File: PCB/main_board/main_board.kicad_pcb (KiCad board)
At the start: 2 copper layers, 57 x 29 mm, 49 parts, among them CN1 XT30PW-M, CN2 XT30PW-M, U1 XT30PW-F, U3 W25N01GVZEIG_C907680, U4 INA226, U5 INA226, U6 RP2040, U7 AZ1117-3.3, X1 X322512MSB4SI

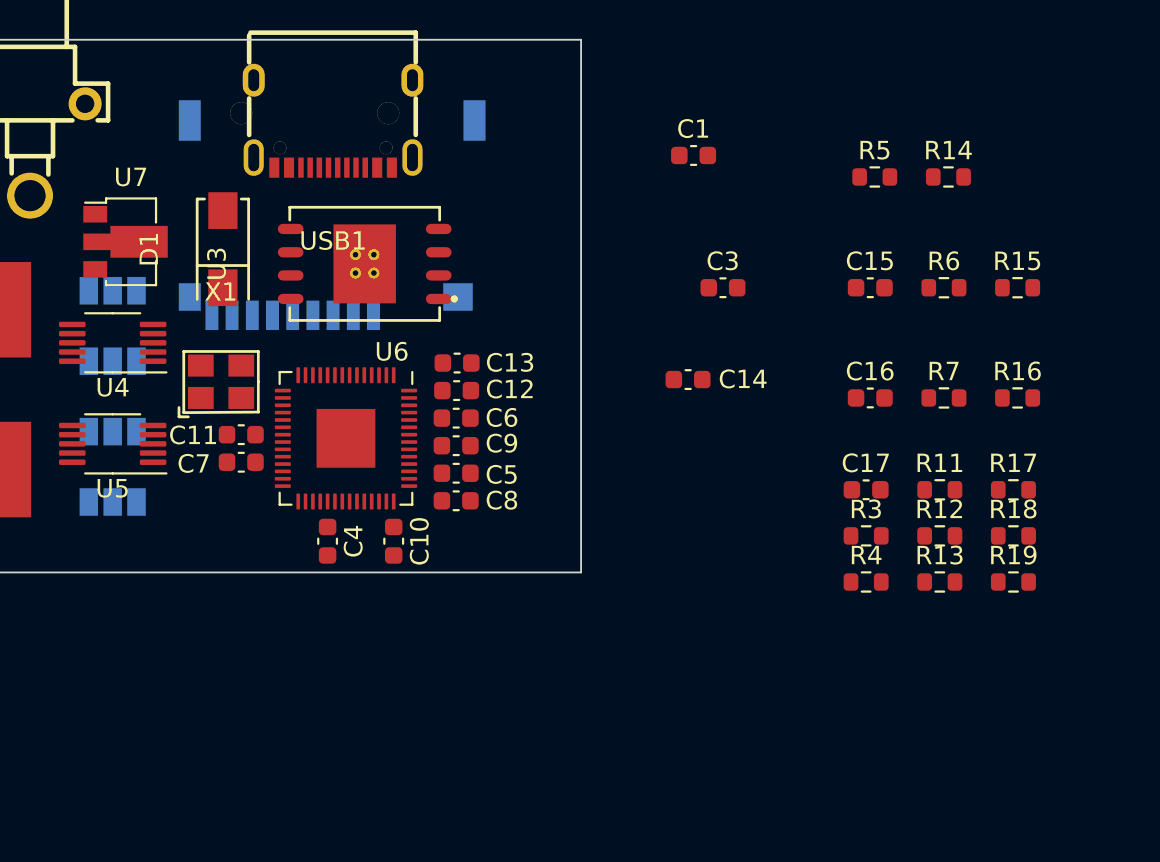
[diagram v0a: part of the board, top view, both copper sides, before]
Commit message: Add EEPROM to mcu; Change R and C to 0402
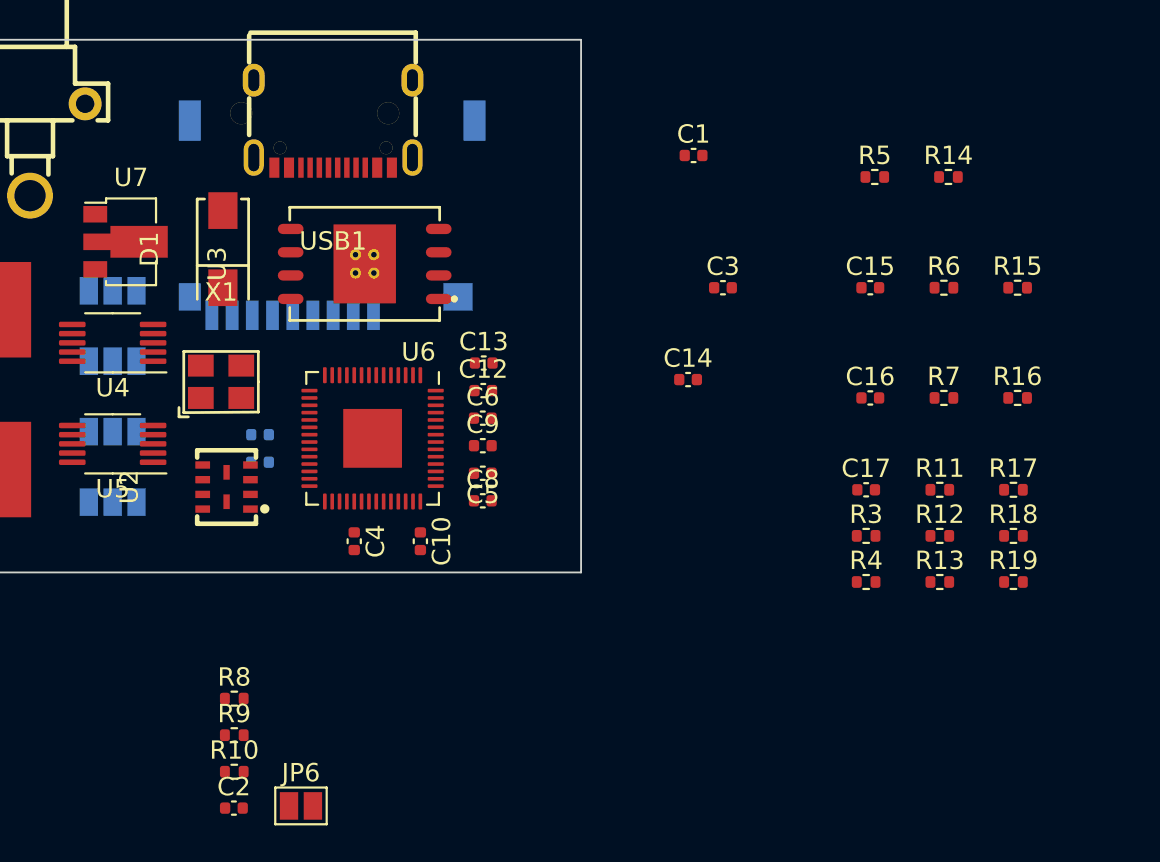
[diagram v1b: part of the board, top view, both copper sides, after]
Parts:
- added C2: 100n, Capacitor_SMD:C_0402_1005Metric, F.Cu at (63.6, 66.3)
- added JP6: SolderJumper_2_Open, Jumper:SolderJumper-2_P1.3mm_Open_Pad1.0x1.5mm, F.Cu at (67.2, 66.2)
- added R10: 1k, Resistor_SMD:R_0402_1005Metric, F.Cu at (63.6, 64.3)
- added R8: 10k, Resistor_SMD:R_0402_1005Metric, F.Cu at (63.6, 60.4)
- added R9: 10k, Resistor_SMD:R_0402_1005Metric, F.Cu at (63.6, 62.4)
- added U2: W25Q32JVUUIQ, pcb_lib:USON-8_L4.0-W3.0-P0.80-BL_WINBOND_UU, F.Cu at (63.2, 48.9)
- C1, C10, C12, C13, C14, C15, C16, C17, C3, C4, C5, C6, C8, C9: footprint Capacitor_SMD:C_0603_1608Metric -> Capacitor_SMD:C_0402_1005Metric
- C11, C7: footprint Capacitor_SMD:C_0603_1608Metric -> Capacitor_SMD:C_0402_1005Metric; moved to B.Cu
- CN1, CN2: footprint easyeda2kicad:CONN-TH_XT30PW-M -> pcb_lib:CONN-TH_XT30PW-M
- Card1: footprint easyeda2kicad:TF-SMD_XKTF-015-N -> pcb_lib:TF-SMD_XKTF-015-N
- D1: footprint easyeda2kicad:SMA_L4.3-W2.5-LS5.0-RD -> pcb_lib:SMA_L4.3-W2.5-LS5.0-RD
- R1, R2: footprint easyeda2kicad:R3920 -> pcb_lib:R3920
- R11, R12, R13, R14, R15, R16, R17, R18, R19, R3, R4, R5, R6, R7: footprint Resistor_SMD:R_0603_1608Metric -> Resistor_SMD:R_0402_1005Metric
- U1: footprint easyeda2kicad:CONN-TH_XT30PW-F-1 -> pcb_lib:CONN-TH_XT30PW-F-1
- U3: footprint easyeda2kicad:WSON-8_L8.0-W6.10-P1.27-BL-EP -> pcb_lib:WSON-8_L8.0-W6.10-P1.27-BL-EP
- USB1: footprint easyeda2kicad:USB-C-SMD_TYPE-C-6PIN-2MD-073 -> pcb_lib:USB-C-SMD_TYPE-C-6PIN-2MD-073
- X1: footprint easyeda2kicad:OSC-SMD_4P-L3.2-W2.5-BL -> pcb_lib:OSC-SMD_4P-L3.2-W2.5-BL
- moved C10 1.45 mm to (73.8, 51.8)
- moved C12 1.45 mm to (77.2, 43.6)
- moved C13 1.45 mm to (77.2, 42.1)
- moved C4 1.45 mm to (70.2, 51.8)
- moved C5 1.45 mm to (77.2, 48.1)
- moved C6 1.45 mm to (77.2, 45.1)
- moved C8 1.45 mm to (77.2, 49.6)
- moved C9 1.45 mm to (77.2, 46.6)
- moved U6 1.45 mm to (71.2, 46.2)
- moved C11 1.02 mm to (65.0, 46.0), turned to 0 degrees
- moved C7 1.02 mm to (65.0, 47.5), turned to 0 degrees
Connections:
- Card1 pad 1: unconnected-(Card1-DAT2-Pad1) -> Net-(Card1-DAT2)
- Card1 pad 8: unconnected-(Card1-DAT1-Pad8) -> Net-(Card1-DAT1)
- U6 pad 51: unconnected-(U6-QSPI_SD3-Pad51) -> SD3
- U6 pad 52: unconnected-(U6-QSPI_SCLK-Pad52) -> SCLK
- U6 pad 53: unconnected-(U6-QSPI_SD0-Pad53) -> SD0
- U6 pad 54: unconnected-(U6-QSPI_SD2-Pad54) -> SD2
- U6 pad 55: unconnected-(U6-QSPI_SD1-Pad55) -> SD1
- U6 pad 56: unconnected-(U6-QSPI_SS-Pad56) -> SS
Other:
- copper layers 2 -> 4

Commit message: Fundamental layout complete
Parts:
- C11: moved to F.Cu
- R8, R9: moved to B.Cu
- moved R6 51.2 mm to (51.5, 44.5)
- moved R5 50.7 mm to (49.4, 44.5)
- moved R3 49.5 mm to (49.4, 42.6)
- moved JP5 48.9 mm to (78.9, 32.5), turned to 90 degrees
- moved R4 47.9 mm to (51.5, 42.6)
- moved R17 44.2 mm to (67.5, 27.3)
- moved R14 42.7 mm to (61.2, 43.1)
- moved R19 42.6 mm to (71.0, 29.8)
- moved R13 41.9 mm to (61.2, 44.2)
- moved C15 41.8 mm to (59.1, 52.5)
- moved R18 41.7 mm to (71.2, 28.6)
- moved R16 41.6 mm to (67.6, 28.8)
- moved R15 40.9 mm to (66.5, 47.6), turned to 90 degrees
- moved R12 39.4 mm to (63.5, 43.1), turned to 180 degrees
- moved R11 38.8 mm to (63.5, 44.2)
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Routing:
- net Net-(U6-XIN): track 0.00 -> 6.39 mm
- net Net-(X1-OSC1): track 0.00 -> 3.26 mm
- net Net-(U6-XOUT): track 0.00 -> 2.21 mm

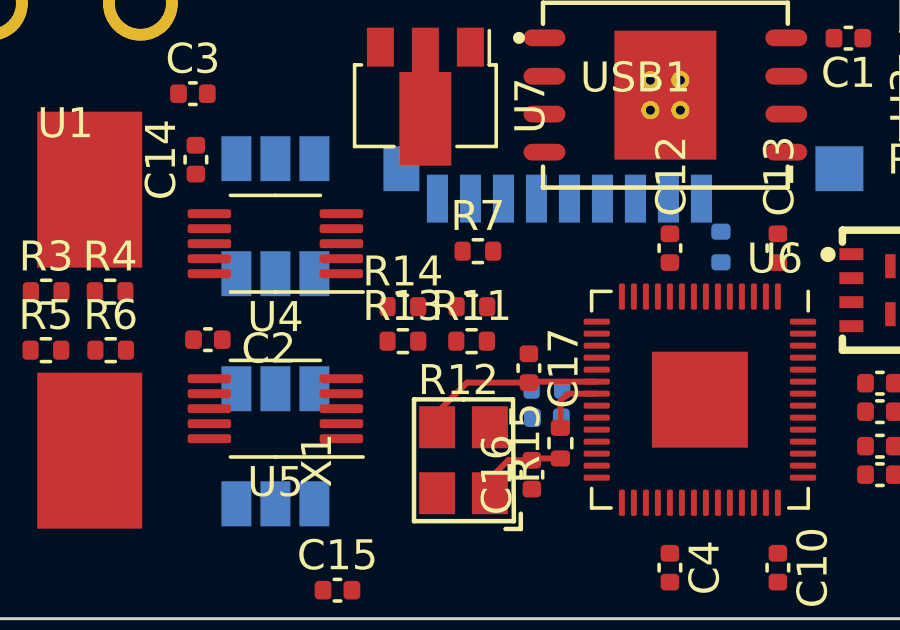
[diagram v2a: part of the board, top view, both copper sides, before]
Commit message: Change IIC0, IIC1 and SPI connection GPIO
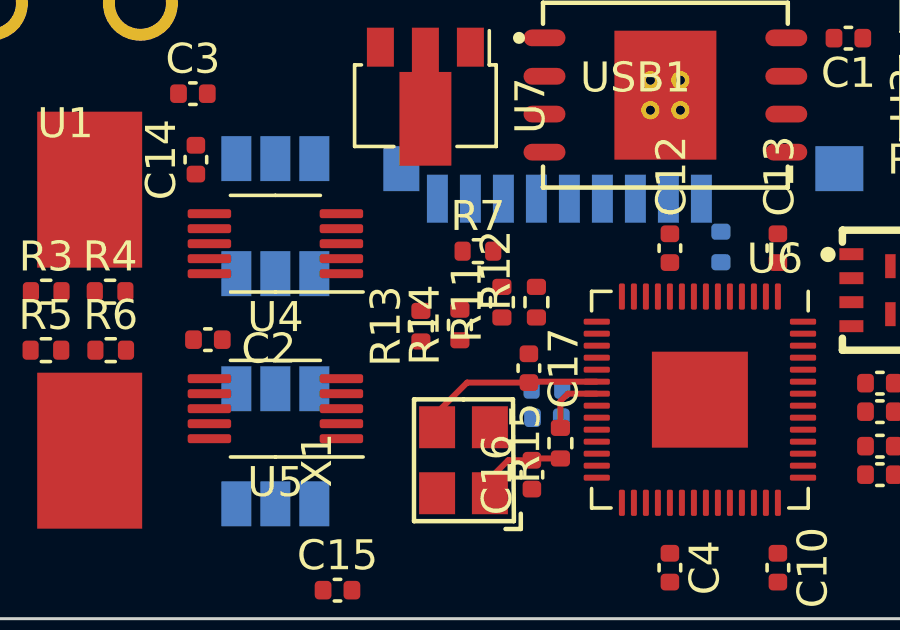
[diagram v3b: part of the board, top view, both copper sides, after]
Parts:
- moved R12 2.16 mm to (65.7, 43.0), turned to -90 degrees
- moved R14 2.00 mm to (63.1, 43.7), turned to 90 degrees
- moved R11 1.65 mm to (64.5, 43.0), turned to 90 degrees
- moved R13 0.78 mm to (61.9, 43.8), turned to 90 degrees
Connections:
- U6 pad 11: MISO1 -> SDA0
- U6 pad 12: CS10 -> SCL0
- U6 pad 13: SCK1 -> unconnected-(U6-GPIO10-Pad13)
- U6 pad 14: MOSI1 -> unconnected-(U6-GPIO11-Pad14)
- U6 pad 16: CS11 -> unconnected-(U6-GPIO13-Pad16)
- U6 pad 3: unconnected-(U6-GPIO1-Pad3) -> CS10
- U6 pad 4: unconnected-(U6-GPIO2-Pad4) -> SCK1
- U6 pad 5: unconnected-(U6-GPIO3-Pad5) -> MOSI1
- U6 pad 6: unconnected-(U6-GPIO4-Pad6) -> MISO1
- U6 pad 7: unconnected-(U6-GPIO5-Pad7) -> CS11
- U6 pad 8: unconnected-(U6-GPIO6-Pad8) -> SDA1
- U6 pad 9: unconnected-(U6-GPIO7-Pad9) -> SCL1

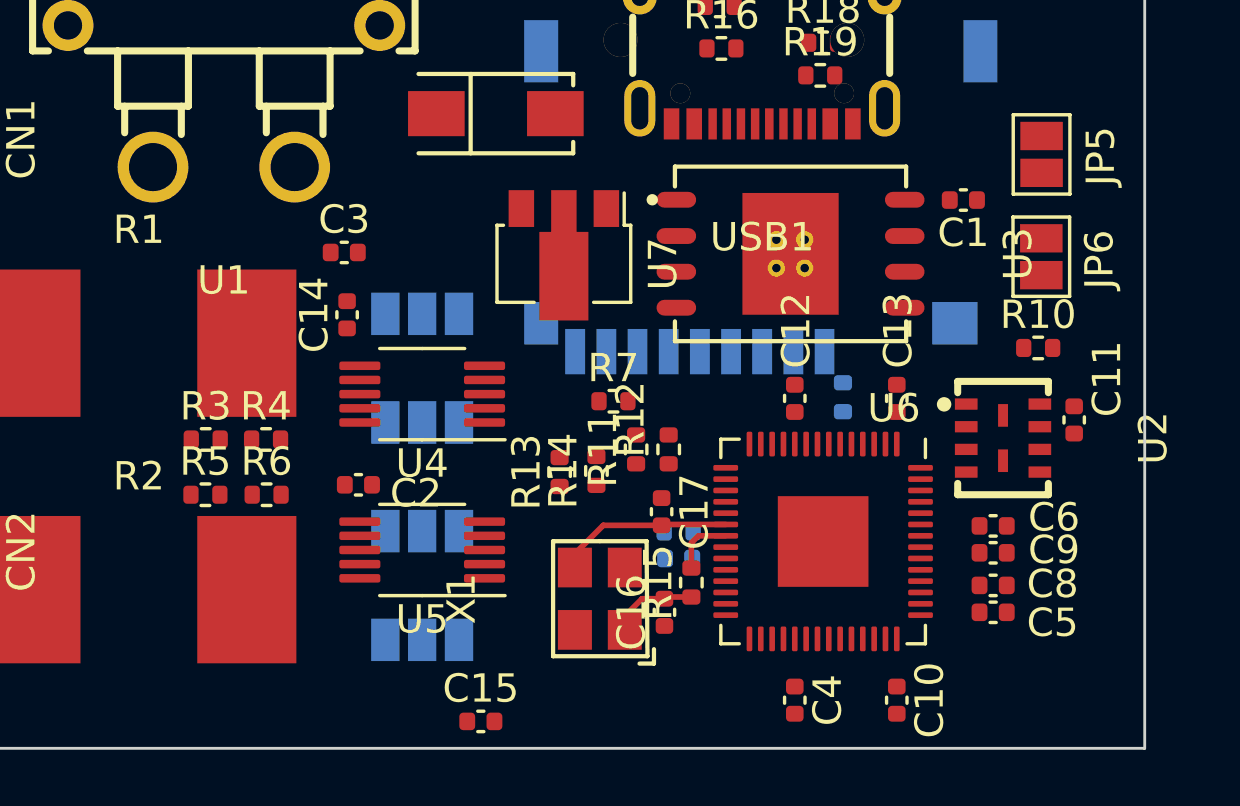
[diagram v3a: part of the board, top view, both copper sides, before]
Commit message: Complete SPI Flash and part of decouple capacitor layout
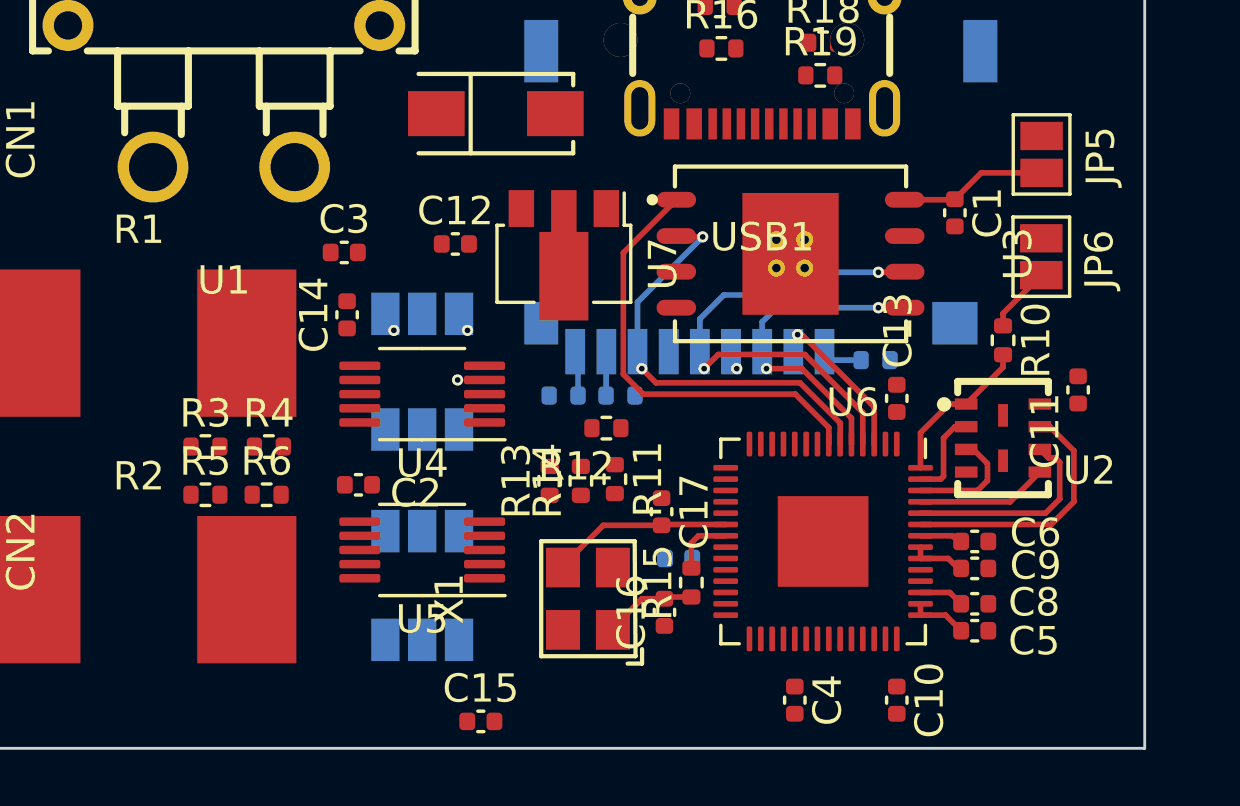
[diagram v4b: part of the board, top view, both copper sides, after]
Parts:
- R7: moved to B.Cu
- moved C12 13.2 mm to (58.2, 35.7), turned to 0 degrees
- moved R9 5.22 mm to (64.0, 41.0)
- moved R12 2.32 mm to (63.5, 42.2), turned to 0 degrees
- moved R7 1.77 mm to (62.0, 41.0), turned to 180 degrees
- moved R8 1.74 mm to (73.0, 39.8), turned to 180 degrees
- moved R11 1.29 mm to (63.8, 44.0), turned to -90 degrees
- moved R10 1.27 mm to (77.5, 39.1), turned to -90 degrees
- moved C11 1.07 mm to (80.2, 40.9), turned to 90 degrees
- moved C5 0.92 mm to (76.5, 48.4)
- moved C8 0.92 mm to (76.5, 49.4)
- moved C6 0.85 mm to (76.5, 46.2)
- moved C9 0.85 mm to (76.5, 47.1)
- moved R14 0.65 mm to (62.6, 44.1)
- moved C1 0.54 mm to (75.8, 34.6), turned to -90 degrees
- moved R13 0.47 mm to (61.5, 44.1)
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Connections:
- C1 pad 1: +3.3V -> Net-(JP5-A)
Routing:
- net SCK1: track 0.00 -> 16.8 mm, vias 0 -> 2
- net CS11: track 0.00 -> 15.5 mm
- net MISO1: track 0.00 -> 14.5 mm, vias 0 -> 2
- net MOSI1: track 0.00 -> 10.9 mm, vias 0 -> 2
- net SD3: track 0.00 -> 9.10 mm
- net SCLK: track 0.00 -> 7.31 mm
- net SS: track 0.00 -> 5.55 mm
- net Net-(JP5-A): track 0.00 -> 5.22 mm
- net CS10: track 0.00 -> 5.07 mm, vias 0 -> 1
- net SD0: track 0.00 -> 4.65 mm
- net +3.3V: track 0.00 -> 4.08 mm, vias 0 -> 1
- net SD2: track 0.00 -> 4.06 mm
- net SD1: track 0.00 -> 3.17 mm
- net +1V1: track 0.00 -> 3.15 mm
- net Net-(JP6-B): track 0.00 -> 2.35 mm
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
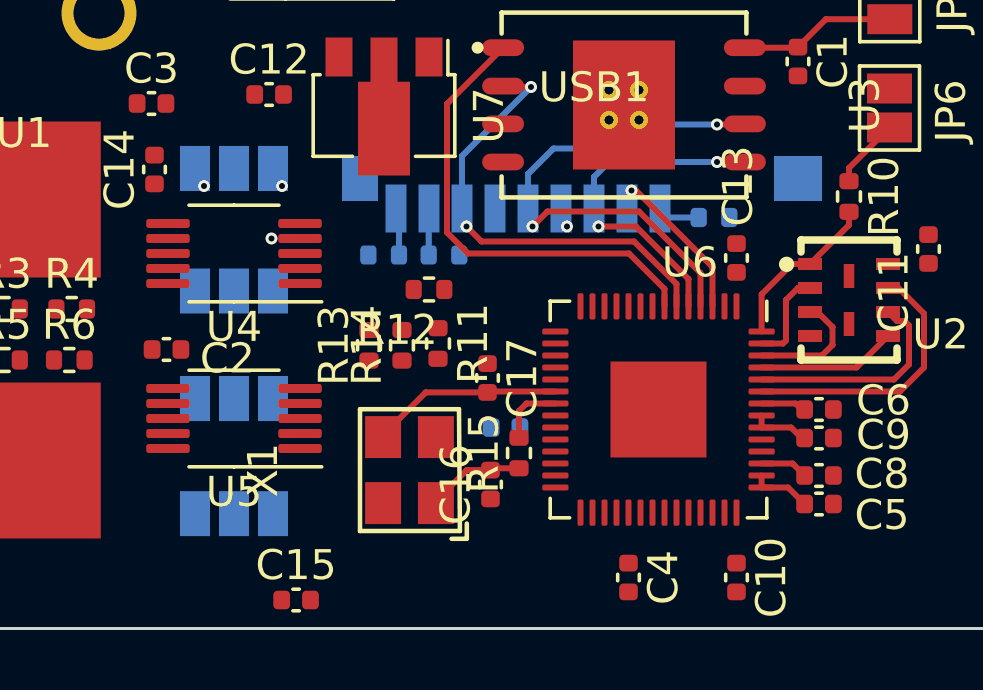
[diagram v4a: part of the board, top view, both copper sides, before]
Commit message: Complete INA226 IIC trace
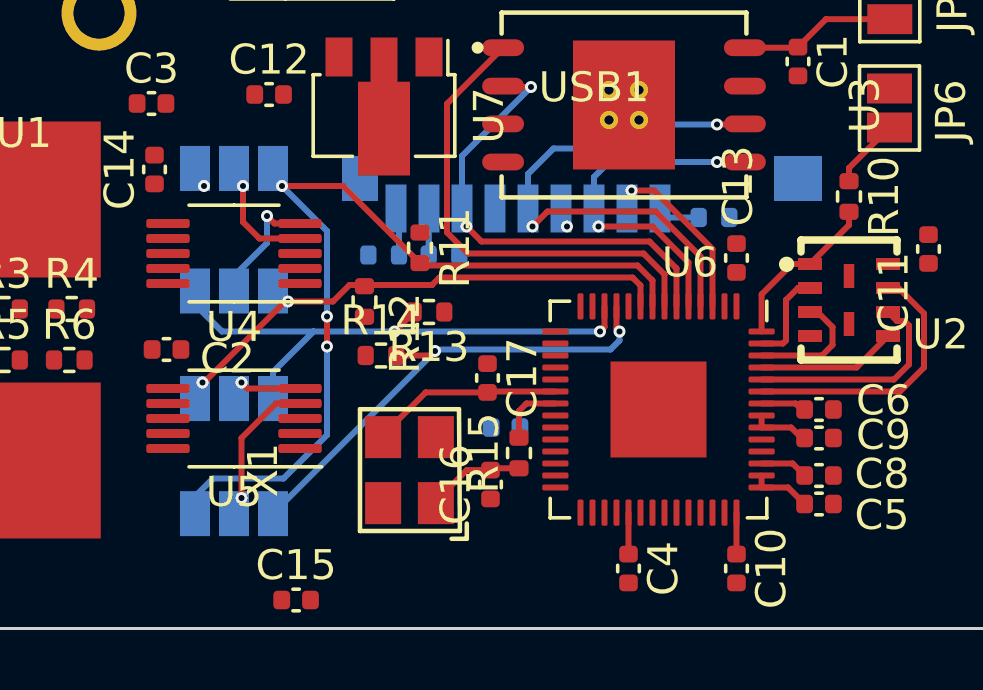
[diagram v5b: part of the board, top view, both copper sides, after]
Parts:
- moved R11 3.25 mm to (63.2, 40.8)
- moved R13 2.29 mm to (63.5, 43.0), turned to 180 degrees
- moved R12 2.19 mm to (61.4, 42.6), turned to 90 degrees
- moved R14 0.78 mm to (61.9, 44.4), turned to 0 degrees
- moved C10 0.30 mm to (73.8, 51.5)
- moved C4 0.30 mm to (70.2, 51.5)
- turned JP2 to 0 degrees
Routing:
- net SDA1: track 0.00 -> 29.3 mm, vias 1 -> 3
- net SCL0: track 0.00 -> 18.9 mm, vias 0 -> 2
- net SCL1: track 0.00 -> 16.9 mm, vias 0 -> 2
- net SDA0: track 0.00 -> 16.5 mm, vias 1 -> 3
- net Net-(JP4-C): track 0.00 -> 4.43 mm, vias 0 -> 1
- net Net-(JP2-C): track 0.00 -> 4.16 mm, vias 0 -> 1
- net Net-(JP1-C): track 0.00 -> 3.33 mm
- net +3.3V: track 4.08 -> 6.84 mm
- net Net-(JP3-C): track 0.00 -> 2.03 mm, vias 0 -> 1
